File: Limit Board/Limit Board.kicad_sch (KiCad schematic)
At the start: 4 parts, among them J1 Conn_01x02_Socket, SW1 SW_DPST_x2

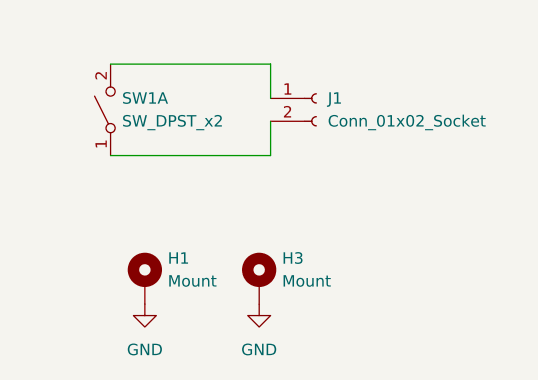
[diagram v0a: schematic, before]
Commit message: Finish schematics and footprint assignments
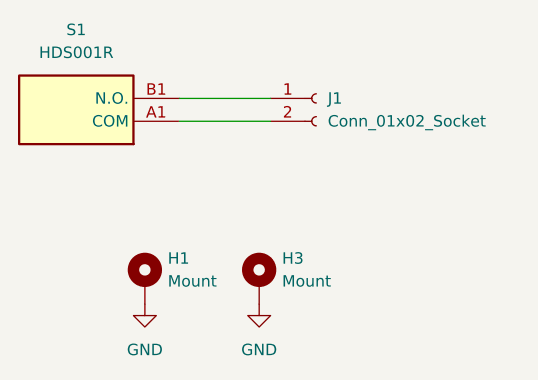
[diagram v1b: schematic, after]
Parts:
- removed SW1: SW_DPST_x2, symbol Switch:SW_DPST_x2
- added S1: HDS001R, HDS001R, symbol HDS001R:HDS001R
- J1: footprint (none) -> Connector_JST:JST_PH_S2B-PH-K_1x02_P2.00mm_Horizontal
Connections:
- net at J1.2 (Pin_2): now also S1.A1 (COM)
- net at J1.1 (Pin_1): now also S1.B1 (N.O.)
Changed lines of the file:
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@@
 	(wire
 		(pts
-			(xy 54.61 90.17) (xy 36.83 90.17)
+			(xy 44.45 93.98) (xy 54.61 93.98)
 		)
 		(stroke
@@
 	(wire
 		(pts
-			(xy 54.61 93.98) (xy 54.61 90.17)
-		)
-		(stroke
-			(width 0)
-			(type default)
-		)
-	)
-	(wire
-		(pts
-			(xy 54.61 96.52) (xy 54.61 100.33)
-		)
-		(stroke
-			(width 0)
-			(type default)
-		)
-	)
-	(wire
-		(pts
-			(xy 54.61 100.33) (xy 36.83 100.33)
+			(xy 44.45 96.52) (xy 54.61 96.52)
 		)
 		(stroke
@@
 	)
 	(symbol
-		(lib_id "Switch:SW_DPST_x2")
-		(at 36.83 95.25 90)
-		(unit 1)
-		(exclude_from_sim no)
-		(in_bom yes)
-		(on_board yes)
-		(dnp no)
-		(fields_autoplaced yes)
-		(property "Reference" "SW1"
-			(at 38.1 93.9799 90)
-			(effects
-				(font
-					(size 1.27 1.27)
-				)
-				(justify right)
-			)
-		)
-		(property "Value" "SW_DPST_x2"
-			(at 38.1 96.5199 90)
-			(effects
-				(font
-					(size 1.27 1.27)
-				)
-				(justify right)
-			)
-		)
-		(property "Footprint" ""
-			(at 36.83 95.25 0)
-			(effects
-				(font
-					(size 1.27 1.27)
-				)
-				(hide yes)
-			)
-		)
-		(property "Datasheet" "~"
-			(at 36.83 95.25 0)
-			(effects
-				(font
-					(size 1.27 1.27)
-				)
-				(hide yes)
-			)
-		)
-		(property "Description" "Single Pole Single Throw (SPST) switch, separate symbol"
-			(at 36.83 95.25 0)
-			(effects
-				(font
-					(size 1.27 1.27)
-				)
-				(hide yes)
-			)
-		)
-		(pin "4"
-		)
-		(pin "1"
-		)
-		(pin "3"
-		)
-		(pin "2"
+		(lib_id "HDS001R:HDS001R")
+		(at 44.45 96.52 180)
+		(unit 1)
+		(exclude_from_sim no)
+		(in_bom yes)
+		(on_board yes)
+		(dnp no)
+		(fields_autoplaced yes)
+		(property "Reference" "S1"
+			(at 33.02 86.36 0)
+			(effects
+				(font
+					(size 1.27 1.27)
+				)
+			)
+		)
+		(property "Value" "HDS001R"
+			(at 33.02 88.9 0)
+			(effects
+				(font
+					(size 1.27 1.27)
+				)
+			)
+		)
+		(property "Footprint" "HDS001R"
+			(at 25.4 1.6 0)
+			(effects
+				(font
+					(size 1.27 1.27)
+				)
+				(justify left top)
+				(hide yes)
+			)
+		)
+		(property "Datasheet" "https://www.ckswitches.com/media/1306/hds.pdf"
+			(at 25.4 -98.4 0)
+			(effects
+				(font
+					(size 1.27 1.27)
+				)
+				(justify left top)
+				(hide yes)
+			)
+		)
+		(property "Description" "Detector Switches Micro Mini Side Actuated Surface Mount Detect Switch"
+			(at 44.45 96.52 0)
+			(effects
+				(font
+					(size 1.27 1.27)
+				)
+				(hide yes)
+			)
+		)
+		(property "Height" "1.4"
+			(at 25.4 -298.4 0)
+			(effects
+				(font
+					(size 1.27 1.27)
+				)
+				(justify left top)
+				(hide yes)
+			)
+		)
+		(property "Mouser Part Number" "611-HDS001R"
+			(at 25.4 -398.4 0)
+			(effects
+				(font
+					(size 1.27 1.27)
+				)
+				(justify left top)
+				(hide yes)
+			)
+		)
+		(property "Mouser Price/Stock" "https://www.mouser.co.uk/ProductDetail/CK/HDS001R?qs=iOhGMg9vv%2F9KIW8Hw0LZ0Q%3D%3D"
+			(at 25.4 -498.4 0)
+			(effects
+				(font
+					(size 1.27 1.27)
+				)
+				(justify left top)
+				(hide yes)
+			)
+		)
+		(property "Manufacturer_Name" "C & K COMPONENTS"
+			(at 25.4 -598.4 0)
+			(effects
+				(font
+					(size 1.27 1.27)
+				)
+				(justify left top)
+				(hide yes)
+			)
+		)
+		(property "Manufacturer_Part_Number" "HDS001R"
+			(at 25.4 -698.4 0)
+			(effects
+				(font
+					(size 1.27 1.27)
+				)
+				(justify left top)
+				(hide yes)
+			)
+		)
+		(pin "B1"
+		)
+		(pin "A1"
 		)
 		(instances
 			(project "Limit Board"
 				(path "/ea187ac2-8767-428a-9ee5-fc9efda02a98"
-					(reference "SW1")
+					(reference "S1")
 					(unit 1)
 				)
@@
 			)
 		)
-		(property "Footprint" ""
+		(property "Footprint" "Connector_JST:JST_PH_S2B-PH-K_1x02_P2.00mm_Horizontal"
 			(at 59.69 93.98 0)
 			(effects

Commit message: Fix unneeded thingy thang on limit
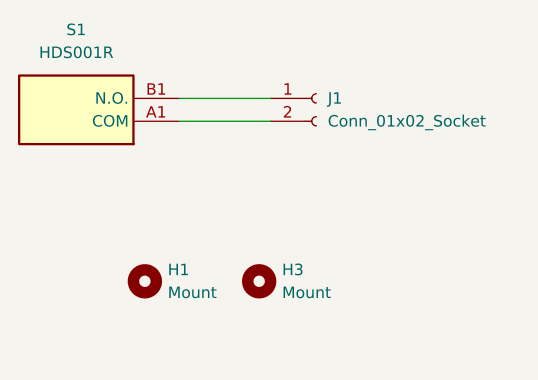
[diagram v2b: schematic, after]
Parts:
- H1, H3: symbol Mechanical:MountingHole_Pad -> Mechanical:MountingHole
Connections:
- removed net GND: H1.1, H3.1
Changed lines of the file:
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@@
 	)
 	(symbol
-		(lib_id "Mechanical:MountingHole_Pad")
+		(lib_id "Mechanical:MountingHole")
 		(at 53.34 114.3 0)
 		(unit 1)
@@
 		(fields_autoplaced yes)
 		(property "Reference" "H3"
-			(at 55.88 111.7599 0)
+			(at 55.88 113.0299 0)
 			(effects
 				(font
@@
 		)
 		(property "Value" "Mount"
-			(at 55.88 114.2999 0)
+			(at 55.88 115.5699 0)
 			(effects
 				(font
@@
 			)
 		)
-		(property "Description" "Mounting Hole with connection"
+		(property "Description" "Mounting Hole without connection"
 			(at 53.34 114.3 0)
 			(effects
@@
 				(hide yes)
 			)
-		)
-		(pin "1"
 		)
 		(instances
@@
 				(path "/ea187ac2-8767-428a-9ee5-fc9efda02a98"
 					(reference "H3")
-					(unit 1)
-				)
-			)
-		)
-	)
-	(symbol
-		(lib_id "power:GND")
-		(at 40.64 116.84 0)
-		(unit 1)
-		(exclude_from_sim no)
-		(in_bom yes)
-		(on_board yes)
-		(dnp no)
-		(fields_autoplaced yes)
-		(property "Reference" "#PWR01"
-			(at 40.64 123.19 0)
-			(effects
-				(font
-					(size 1.27 1.27)
-				)
-				(hide yes)
-			)
-		)
-		(property "Value" "GND"
-			(at 40.64 121.92 0)
-			(effects
-				(font
-					(size 1.27 1.27)
-				)
-			)
-		)
-		(property "Footprint" ""
-			(at 40.64 116.84 0)
-			(effects
-				(font
-					(size 1.27 1.27)
-				)
-				(hide yes)
-			)
-		)
-		(property "Datasheet" ""
-			(at 40.64 116.84 0)
-			(effects
-				(font
-					(size 1.27 1.27)
-				)
-				(hide yes)
-			)
-		)
-		(property "Description" "Power symbol creates a global label with name \"GND\" , ground"
-			(at 40.64 116.84 0)
-			(effects
-				(font
-					(size 1.27 1.27)
-				)
-				(hide yes)
-			)
-		)
-		(pin "1"
-		)
-		(instances
-			(project "Limit Board"
-				(path "/ea187ac2-8767-428a-9ee5-fc9efda02a98"
-					(reference "#PWR01")
 					(unit 1)
 				)
@@
 	)
 	(symbol
-		(lib_id "power:GND")
-		(at 53.34 116.84 0)
-		(unit 1)
-		(exclude_from_sim no)
-		(in_bom yes)
-		(on_board yes)
-		(dnp no)
-		(fields_autoplaced yes)
-		(property "Reference" "#PWR03"
-			(at 53.34 123.19 0)
-			(effects
-				(font
-					(size 1.27 1.27)
-				)
-				(hide yes)
-			)
-		)
-		(property "Value" "GND"
-			(at 53.34 121.92 0)
-			(effects
-				(font
-					(size 1.27 1.27)
-				)
-			)
-		)
-		(property "Footprint" ""
-			(at 53.34 116.84 0)
-			(effects
-				(font
-					(size 1.27 1.27)
-				)
-				(hide yes)
-			)
-		)
-		(property "Datasheet" ""
-			(at 53.34 116.84 0)
-			(effects
-				(font
-					(size 1.27 1.27)
-				)
-				(hide yes)
-			)
-		)
-		(property "Description" "Power symbol creates a global label with name \"GND\" , ground"
-			(at 53.34 116.84 0)
-			(effects
-				(font
-					(size 1.27 1.27)
-				)
-				(hide yes)
-			)
-		)
-		(pin "1"
-		)
-		(instances
-			(project "Limit Board"
-				(path "/ea187ac2-8767-428a-9ee5-fc9efda02a98"
-					(reference "#PWR03")
-					(unit 1)
-				)
-			)
-		)
-	)
-	(symbol
 		(lib_id "Connector:Conn_01x02_Socket")
 		(at 59.69 93.98 0)
@@
 	)
 	(symbol
-		(lib_id "Mechanical:MountingHole_Pad")
+		(lib_id "Mechanical:MountingHole")
 		(at 40.64 114.3 0)
 		(unit 1)
@@
 		(fields_autoplaced yes)
 		(property "Reference" "H1"
-			(at 43.18 111.7599 0)
+			(at 43.18 113.0299 0)
 			(effects
 				(font
@@
 		)
 		(property "Value" "Mount"
-			(at 43.18 114.2999 0)
+			(at 43.18 115.5699 0)
 			(effects
 				(font
@@
 			)
 		)
-		(property "Description" "Mounting Hole with connection"
+		(property "Description" "Mounting Hole without connection"
 			(at 40.64 114.3 0)
 			(effects
@@
 			)
 		)
-		(pin "1"
-		)
 		(instances

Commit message: Fix edge cuts
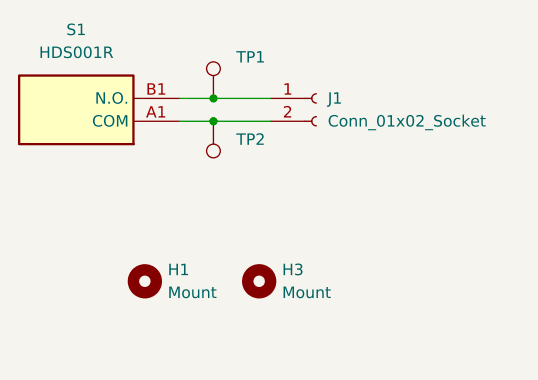
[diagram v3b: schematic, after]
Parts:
- added TP1, TP2: TestPoint, TestPoint:TestPoint_Pad_1.5x1.5mm, symbol Connector:TestPoint
- S1: footprint HDS001R -> Canhw:HDS001R
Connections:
- net at J1.2 (Pin_2), S1.A1 (COM): now also TP2.1
- net at J1.1 (Pin_1), S1.B1 (N.O.): now also TP1.1
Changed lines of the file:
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@@
 	(generator_version "8.0")
 	(paper "A4")
+	(junction
+		(at 48.26 93.98)
+		(diameter 0)
+		(color 0 0 0 0)
+	)
+	(junction
+		(at 48.26 96.52)
+		(diameter 0)
+		(color 0 0 0 0)
+	)
 	(wire
 		(pts
-			(xy 44.45 93.98) (xy 54.61 93.98)
+			(xy 48.26 96.52) (xy 54.61 96.52)
 		)
 		(stroke
@@
 	(wire
 		(pts
-			(xy 44.45 96.52) (xy 54.61 96.52)
+			(xy 48.26 93.98) (xy 54.61 93.98)
+		)
+		(stroke
+			(width 0)
+			(type default)
+		)
+	)
+	(wire
+		(pts
+			(xy 44.45 93.98) (xy 48.26 93.98)
+		)
+		(stroke
+			(width 0)
+			(type default)
+		)
+	)
+	(wire
+		(pts
+			(xy 44.45 96.52) (xy 48.26 96.52)
 		)
 		(stroke
@@
 	)
 	(symbol
+		(lib_id "Connector:TestPoint")
+		(at 48.26 93.98 0)
+		(unit 1)
+		(exclude_from_sim no)
+		(in_bom yes)
+		(on_board yes)
+		(dnp no)
+		(fields_autoplaced yes)
+		(property "Reference" "TP1"
+			(at 50.8 89.4079 0)
+			(effects
+				(font
+					(size 1.27 1.27)
+				)
+				(justify left)
+			)
+		)
+		(property "Value" "TestPoint"
+			(at 50.8 91.9479 0)
+			(effects
+				(font
+					(size 1.27 1.27)
+				)
+				(justify left)
+				(hide yes)
+			)
+		)
+		(property "Footprint" "TestPoint:TestPoint_Pad_1.5x1.5mm"
+			(at 53.34 93.98 0)
+			(effects
+				(font
+					(size 1.27 1.27)
+				)
+				(hide yes)
+			)
+		)
+		(property "Datasheet" "~"
+			(at 53.34 93.98 0)
+			(effects
+				(font
+					(size 1.27 1.27)
+				)
+				(hide yes)
+			)
+		)
+		(property "Description" "test point"
+			(at 48.26 93.98 0)
+			(effects
+				(font
+					(size 1.27 1.27)
+				)
+				(hide yes)
+			)
+		)
+		(pin "1"
+		)
+		(instances
+			(project "Limit Board"
+				(path "/ea187ac2-8767-428a-9ee5-fc9efda02a98"
+					(reference "TP1")
+					(unit 1)
+				)
+			)
+		)
+	)
+	(symbol
 		(lib_id "HDS001R:HDS001R")
 		(at 44.45 96.52 180)
@@
 			)
 		)
-		(property "Footprint" "HDS001R"
+		(property "Footprint" "Canhw:HDS001R"
 			(at 25.4 1.6 0)
 			(effects
@@
 					(unit 1)
 				)
+			)
+		)
+	)
+	(symbol
+		(lib_id "Connector:TestPoint")
+		(at 48.26 96.52 180)
+		(unit 1)
+		(exclude_from_sim no)
+		(in_bom yes)
+		(on_board yes)
+		(dnp no)
+		(fields_autoplaced yes)
+		(property "Reference" "TP2"
+			(at 50.8 98.5519 0)
+			(effects
+				(font
+					(size 1.27 1.27)
+				)
+				(justify right)
+			)
+		)
+		(property "Value" "TestPoint"
+			(at 50.8 101.0919 0)
+			(effects
+				(font
+					(size 1.27 1.27)
+				)
+				(justify right)
+				(hide yes)
+			)
+		)
+		(property "Footprint" "TestPoint:TestPoint_Pad_1.5x1.5mm"
+			(at 43.18 96.52 0)
+			(effects
+				(font
+					(size 1.27 1.27)
+				)
+				(hide yes)
+			)
+		)
+		(property "Datasheet" "~"
+			(at 43.18 96.52 0)
+			(effects
+				(font
+					(size 1.27 1.27)
+				)
+				(hide yes)
+			)
+		)
+		(property "Description" "test point"
+			(at 48.26 96.52 0)
+			(effects
+				(font
+					(size 1.27 1.27)
+				)
+				(hide yes)
+			)
+		)
+		(pin "1"
+		)
+		(instances
+			(project "Limit Board"
+				(path "/ea187ac2-8767-428a-9ee5-fc9efda02a98"
+					(reference "TP2")
+					(unit 1)
+				)
